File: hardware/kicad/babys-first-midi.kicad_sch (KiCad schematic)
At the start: 22 parts, among them J1 RJ45_FEMALE, J2 TRS TYPE A, Q1 IRLZ44N, Q2 IRLZ44N, Q3 IRLZ44N, Q4 IRLZ44N, Q5 IRLZ44N, U1 Pimoroni Tiny 2350

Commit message: Assign prototype through-hole footprints
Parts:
- J1: footprint (none) -> Connector_RJ:RJ45_Amphenol_RJHSE538X
- J2: footprint (none) -> Connector_Audio:Jack_3.5mm_CUI_SJ1-3523N_Horizontal
- Q1, Q2, Q3, Q4, Q5: footprint (none) -> Package_TO_SOT_THT:TO-220-3_Vertical
- R1, R10, R11, R12, R2, R3, R4, R5, R6, R7, R8, R9: footprint (none) -> Resistor_THT:R_Axial_DIN0207_L6.3mm_D2.5mm_P10.16mm_Horizontal
- RV1, RV2: footprint (none) -> Potentiometer_THT:Potentiometer_Alps_RK09K_Single_Horizontal
- U1: footprint (none) -> BFM:Tiny2350_Module

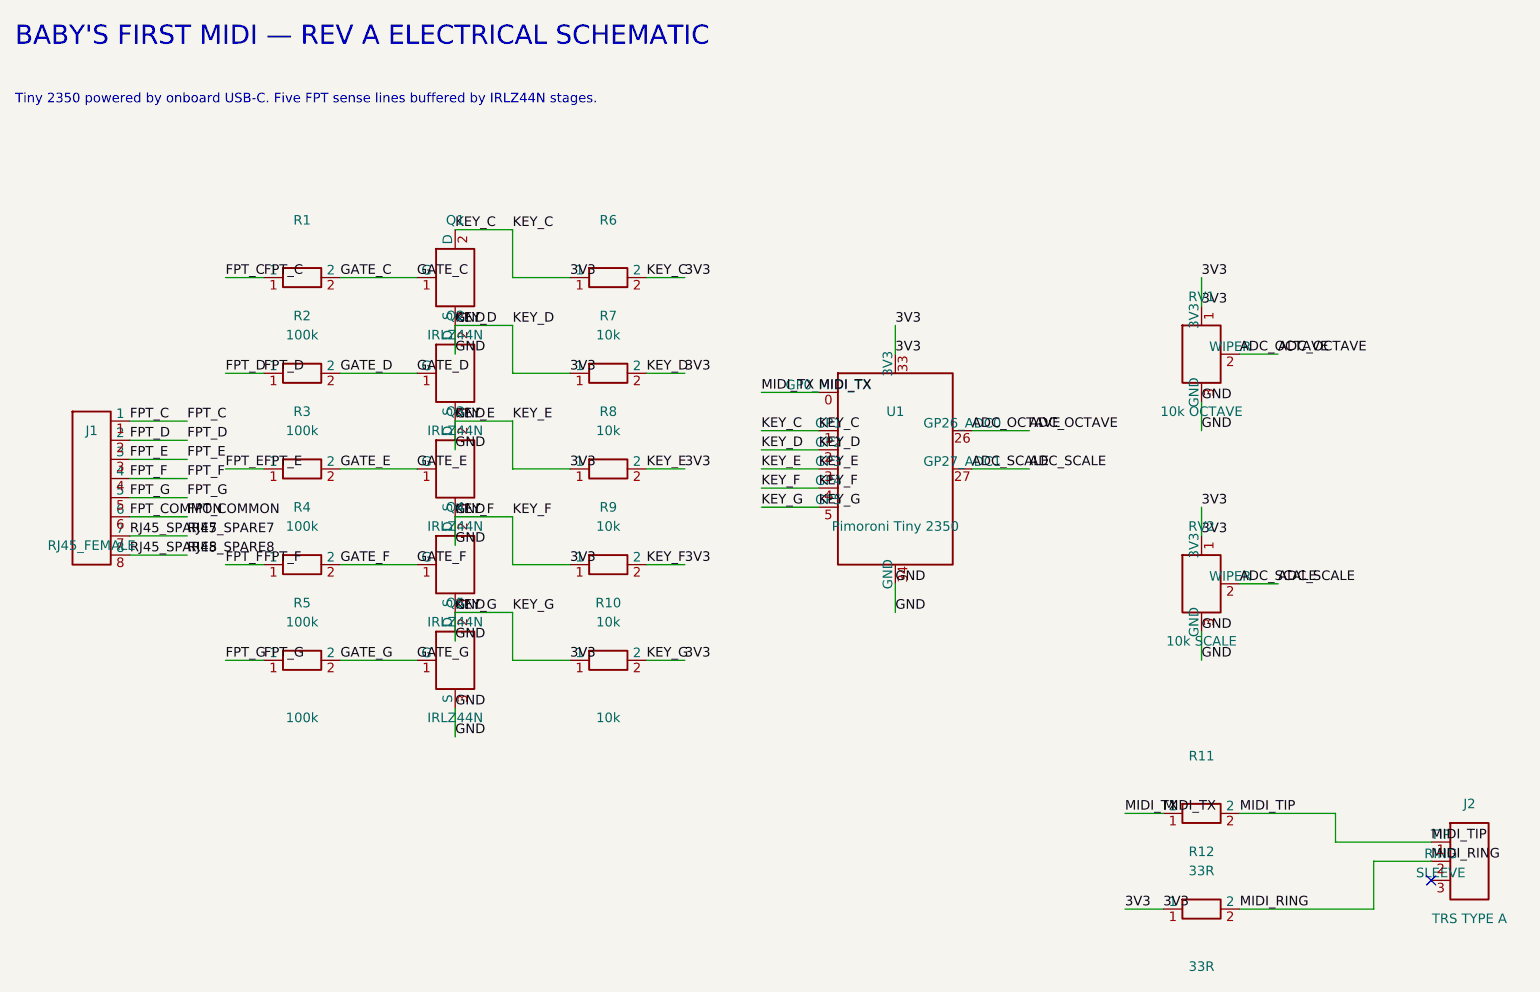
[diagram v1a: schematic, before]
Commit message: Replace input MOSFETs with through-hole 2N7000 TO-92 parts
Replace Q1-Q5 IRLZ44N packages with local TO-92 footprints at 2.54 mm lead spacing and standard KiCad 3D models. Remap source/gate/drain to pins 1/2/3 in PCB and embedded schematic symbol while preserving connections by function. Reroute and refill the PCB.

Verified all component PCB net assignments and before/after schematic netlists with the functional pin remap. KiCad 10.0.6 DRC: zero violations, zero unconnected items.
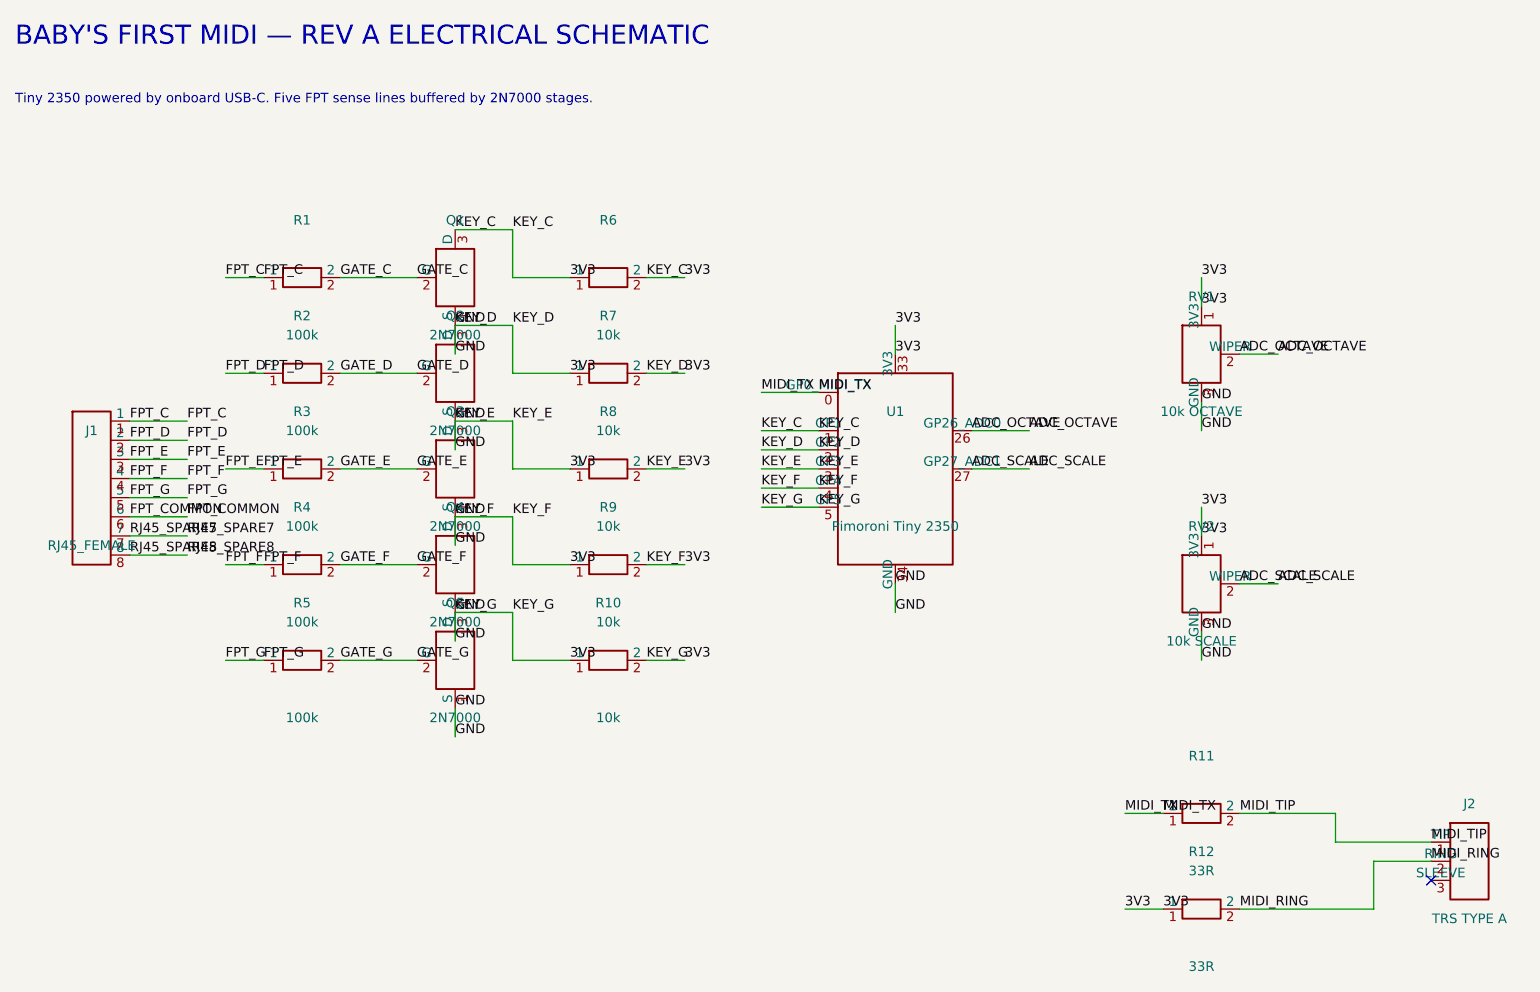
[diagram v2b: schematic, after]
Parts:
- Q1, Q2, Q3, Q4, Q5: value IRLZ44N -> 2N7000; footprint Package_TO_SOT_THT:TO-220-3_Vertical -> BFM:TO-92_2N7000_SGD
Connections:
- net 3V3: now also Q1.1 (S), Q2.1 (S), Q3.1 (S), Q4.1 (S), Q5.1 (S); no longer Q1.2 (D), Q2.2 (D), Q3.2 (D), Q4.2 (D), Q5.2 (D)
- net GATE_C: now also Q1.2 (G); no longer Q1.1 (G)
- net GATE_D: now also Q2.2 (G); no longer Q2.1 (G)
- net GATE_E: now also Q3.2 (G); no longer Q3.1 (G)
- net GATE_F: now also Q4.2 (G); no longer Q4.1 (G)
- net GATE_G: now also Q5.2 (G); no longer Q5.1 (G)
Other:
- note added: "Tiny 2350 powered by onboard USB-C. Five FPT sense lines buffered by 2N7000 stages."
- note removed: "Tiny 2350 powered by onboard USB-C. Five FPT sense lines buffered by IRLZ44N stages."
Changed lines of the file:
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@@
   (text "BABY'S FIRST MIDI — REV A ELECTRICAL SCHEMATIC" (exclude_from_sim no) (at 20.32 15.24 0)
     (effects (font (size 2.54 2.54) (thickness 0.5)) (justify left bottom)))
-  (text "Tiny 2350 powered by onboard USB-C. Five FPT sense lines buffered by IRLZ44N stages." (exclude_from_sim no) (at 20.32 22.86 0)
+  (text "Tiny 2350 powered by onboard USB-C. Five FPT sense lines buffered by 2N7000 stages." (exclude_from_sim no) (at 20.32 22.86 0)
     (effects (font (size 1.27 1.27)) (justify left bottom)))
   (symbol (lib_id "BFM:CONN8") (at 30.48 73.66 0) (unit 1) (body_style 1) (exclude_from_sim no) (in_bom yes) (on_board yes) (in_pos_files yes) (dnp no)
@@
   (symbol (lib_id "BFM:NMOS") (at 78.74 45.72 0) (unit 1) (body_style 1) (exclude_from_sim no) (in_bom yes) (on_board yes) (in_pos_files yes) (dnp no)
         (property "Reference" "Q1" (at 78.74 38.1 0) (effects (font (size 1.27 1.27))))
-        (property "Value" "IRLZ44N" (at 78.74 53.339999999999996 0) (effects (font (size 1.27 1.27))))
-        (property "Footprint" "Package_TO_SOT_THT:TO-220-3_Vertical" (at 78.74 45.72 0) (hide yes) (effects (font (size 1.27 1.27))))
+        (property "Value" "2N7000" (at 78.74 53.339999999999996 0) (effects (font (size 1.27 1.27))))
+        (property "Footprint" "BFM:TO-92_2N7000_SGD" (at 78.74 45.72 0) (hide yes) (effects (font (size 1.27 1.27))))
         (property "Datasheet" "" (at 78.74 45.72 0) (hide yes) (effects (font (size 1.27 1.27))))
         (property "Description" "FPT input buffer" (at 78.74 45.72 0) (hide yes) (effects (font (size 1.27 1.27))))
-        (pin "1")
         (pin "2")
         (pin "3")
+        (pin "1")
         (instances (project "babys-first-midi" (path "/b1f00000-0000-4000-8000-000000000001" (reference "Q1") (unit 1))))
       )
@@
   (symbol (lib_id "BFM:NMOS") (at 78.74 58.42 0) (unit 1) (body_style 1) (exclude_from_sim no) (in_bom yes) (on_board yes) (in_pos_files yes) (dnp no)
         (property "Reference" "Q2" (at 78.74 50.800000000000004 0) (effects (font (size 1.27 1.27))))
-        (property "Value" "IRLZ44N" (at 78.74 66.04 0) (effects (font (size 1.27 1.27))))
-        (property "Footprint" "Package_TO_SOT_THT:TO-220-3_Vertical" (at 78.74 58.42 0) (hide yes) (effects (font (size 1.27 1.27))))
+        (property "Value" "2N7000" (at 78.74 66.04 0) (effects (font (size 1.27 1.27))))
+        (property "Footprint" "BFM:TO-92_2N7000_SGD" (at 78.74 58.42 0) (hide yes) (effects (font (size 1.27 1.27))))
         (property "Datasheet" "" (at 78.74 58.42 0) (hide yes) (effects (font (size 1.27 1.27))))
         (property "Description" "FPT input buffer" (at 78.74 58.42 0) (hide yes) (effects (font (size 1.27 1.27))))
-        (pin "1")
         (pin "2")
         (pin "3")
+        (pin "1")
         (instances (project "babys-first-midi" (path "/b1f00000-0000-4000-8000-000000000001" (reference "Q2") (unit 1))))
       )
@@
   (symbol (lib_id "BFM:NMOS") (at 78.74 71.12 0) (unit 1) (body_style 1) (exclude_from_sim no) (in_bom yes) (on_board yes) (in_pos_files yes) (dnp no)
         (property "Reference" "Q3" (at 78.74 63.50000000000001 0) (effects (font (size 1.27 1.27))))
-        (property "Value" "IRLZ44N" (at 78.74 78.74000000000001 0) (effects (font (size 1.27 1.27))))
-        (property "Footprint" "Package_TO_SOT_THT:TO-220-3_Vertical" (at 78.74 71.12 0) (hide yes) (effects (font (size 1.27 1.27))))
+        (property "Value" "2N7000" (at 78.74 78.74000000000001 0) (effects (font (size 1.27 1.27))))
+        (property "Footprint" "BFM:TO-92_2N7000_SGD" (at 78.74 71.12 0) (hide yes) (effects (font (size 1.27 1.27))))
         (property "Datasheet" "" (at 78.74 71.12 0) (hide yes) (effects (font (size 1.27 1.27))))
         (property "Description" "FPT input buffer" (at 78.74 71.12 0) (hide yes) (effects (font (size 1.27 1.27))))
-        (pin "1")
         (pin "2")
         (pin "3")
+        (pin "1")
         (instances (project "babys-first-midi" (path "/b1f00000-0000-4000-8000-000000000001" (reference "Q3") (unit 1))))
       )
@@
   (symbol (lib_id "BFM:NMOS") (at 78.74 83.82 0) (unit 1) (body_style 1) (exclude_from_sim no) (in_bom yes) (on_board yes) (in_pos_files yes) (dnp no)
         (property "Reference" "Q4" (at 78.74 76.19999999999999 0) (effects (font (size 1.27 1.27))))
-        (property "Value" "IRLZ44N" (at 78.74 91.44 0) (effects (font (size 1.27 1.27))))
-        (property "Footprint" "Package_TO_SOT_THT:TO-220-3_Vertical" (at 78.74 83.82 0) (hide yes) (effects (font (size 1.27 1.27))))
+        (property "Value" "2N7000" (at 78.74 91.44 0) (effects (font (size 1.27 1.27))))
+        (property "Footprint" "BFM:TO-92_2N7000_SGD" (at 78.74 83.82 0) (hide yes) (effects (font (size 1.27 1.27))))
         (property "Datasheet" "" (at 78.74 83.82 0) (hide yes) (effects (font (size 1.27 1.27))))
         (property "Description" "FPT input buffer" (at 78.74 83.82 0) (hide yes) (effects (font (size 1.27 1.27))))
-        (pin "1")
         (pin "2")
         (pin "3")
+        (pin "1")
         (instances (project "babys-first-midi" (path "/b1f00000-0000-4000-8000-000000000001" (reference "Q4") (unit 1))))
       )
@@
   (symbol (lib_id "BFM:NMOS") (at 78.74 96.52 0) (unit 1) (body_style 1) (exclude_from_sim no) (in_bom yes) (on_board yes) (in_pos_files yes) (dnp no)
         (property "Reference" "Q5" (at 78.74 88.89999999999999 0) (effects (font (size 1.27 1.27))))
-        (property "Value" "IRLZ44N" (at 78.74 104.14 0) (effects (font (size 1.27 1.27))))
-        (property "Footprint" "Package_TO_SOT_THT:TO-220-3_Vertical" (at 78.74 96.52 0) (hide yes) (effects (font (size 1.27 1.27))))
+        (property "Value" "2N7000" (at 78.74 104.14 0) (effects (font (size 1.27 1.27))))
+        (property "Footprint" "BFM:TO-92_2N7000_SGD" (at 78.74 96.52 0) (hide yes) (effects (font (size 1.27 1.27))))
         (property "Datasheet" "" (at 78.74 96.52 0) (hide yes) (effects (font (size 1.27 1.27))))
         (property "Description" "FPT input buffer" (at 78.74 96.52 0) (hide yes) (effects (font (size 1.27 1.27))))
-        (pin "1")
         (pin "2")
         (pin "3")
+        (pin "1")
         (instances (project "babys-first-midi" (path "/b1f00000-0000-4000-8000-000000000001" (reference "Q5") (unit 1))))
       )
